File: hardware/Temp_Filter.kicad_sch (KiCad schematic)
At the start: 9 parts, among them U7 TLV9062xD

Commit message: schem except BQ
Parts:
- added C22: 1uF, Capacitor_SMD:C_0805_2012Metric_Pad1.18x1.45mm_HandSolder, symbol Device:C
- added C48: 1.2uF, Capacitor_SMD:C_0805_2012Metric_Pad1.18x1.45mm_HandSolder, symbol Device:C
- added R44: 27kΩ, Resistor_SMD:R_0603_1608Metric_Pad0.98x0.95mm_HandSolder, symbol Device:R
- added R45, R46: 2.7kΩ, Resistor_SMD:R_0603_1608Metric_Pad0.98x0.95mm_HandSolder, symbol Device:R
- added R9: 8.2kΩ, Resistor_SMD:R_0603_1608Metric_Pad0.98x0.95mm_HandSolder, symbol Device:R
- added TP12: TP_TempOut, TestPoint:TestPoint_Pad_1.0x1.0mm, symbol Connector:TestPoint
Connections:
- net GNDA: now also C22.2, R45.1
- net VDDA renamed 3.3VA
- net tempIn: no longer names the net of U7.3 (+)
- net tempIn: now also C22.1, R44.2
- net tempOut renamed tempOut_2
- new net: C48.1, R44.1, R9.2
- new net: R45.2, R46.1, U7.2 (-)
- new net tempIn_1: R9.1
- new net tempIn_2: R8.1
- new net tempOut_1: C48.2, R46.2, TP12.1, U7.1
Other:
- moved on the sheet: C20, C21, C47, R41, R42, R43, R8, TP11, U7B, U7C

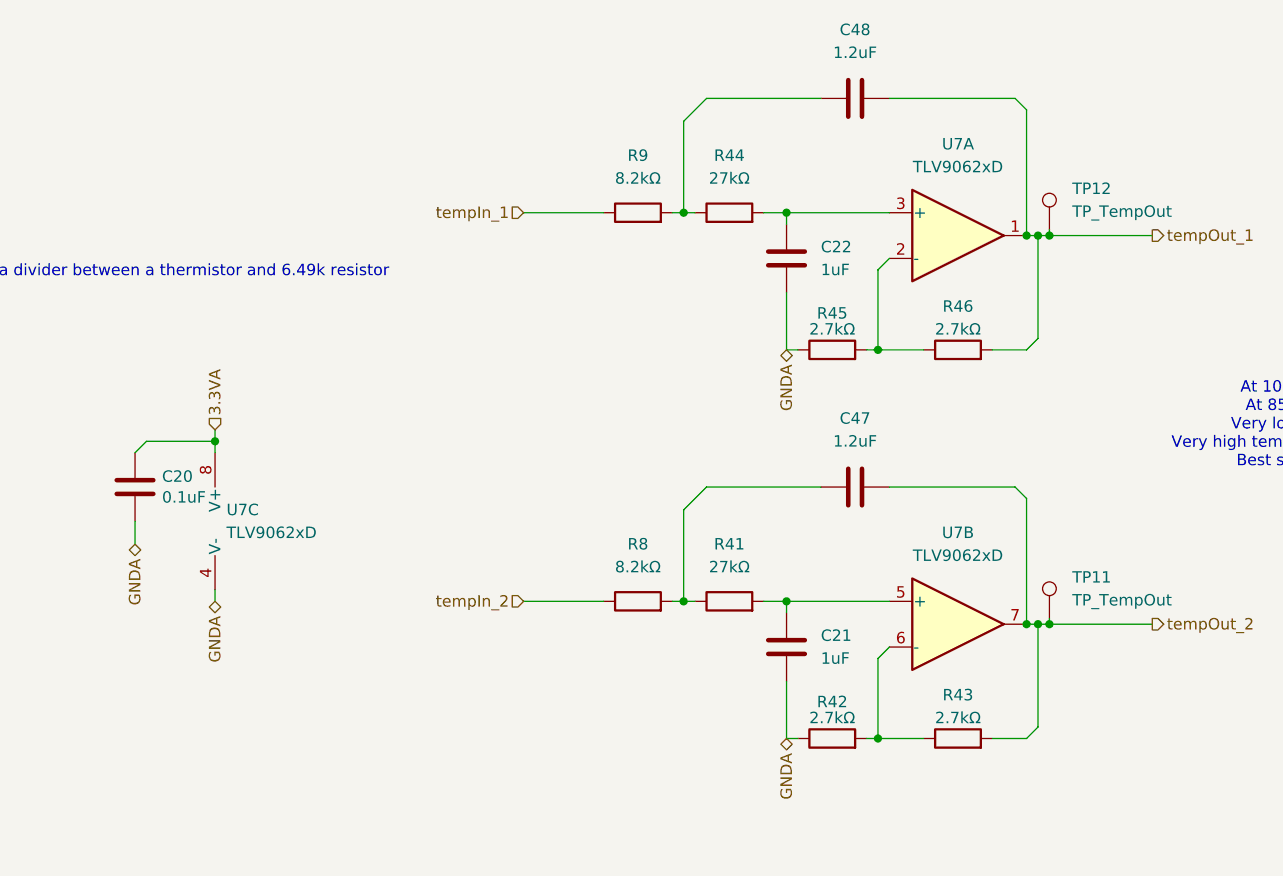
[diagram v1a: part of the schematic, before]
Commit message: New BMS arch and IC
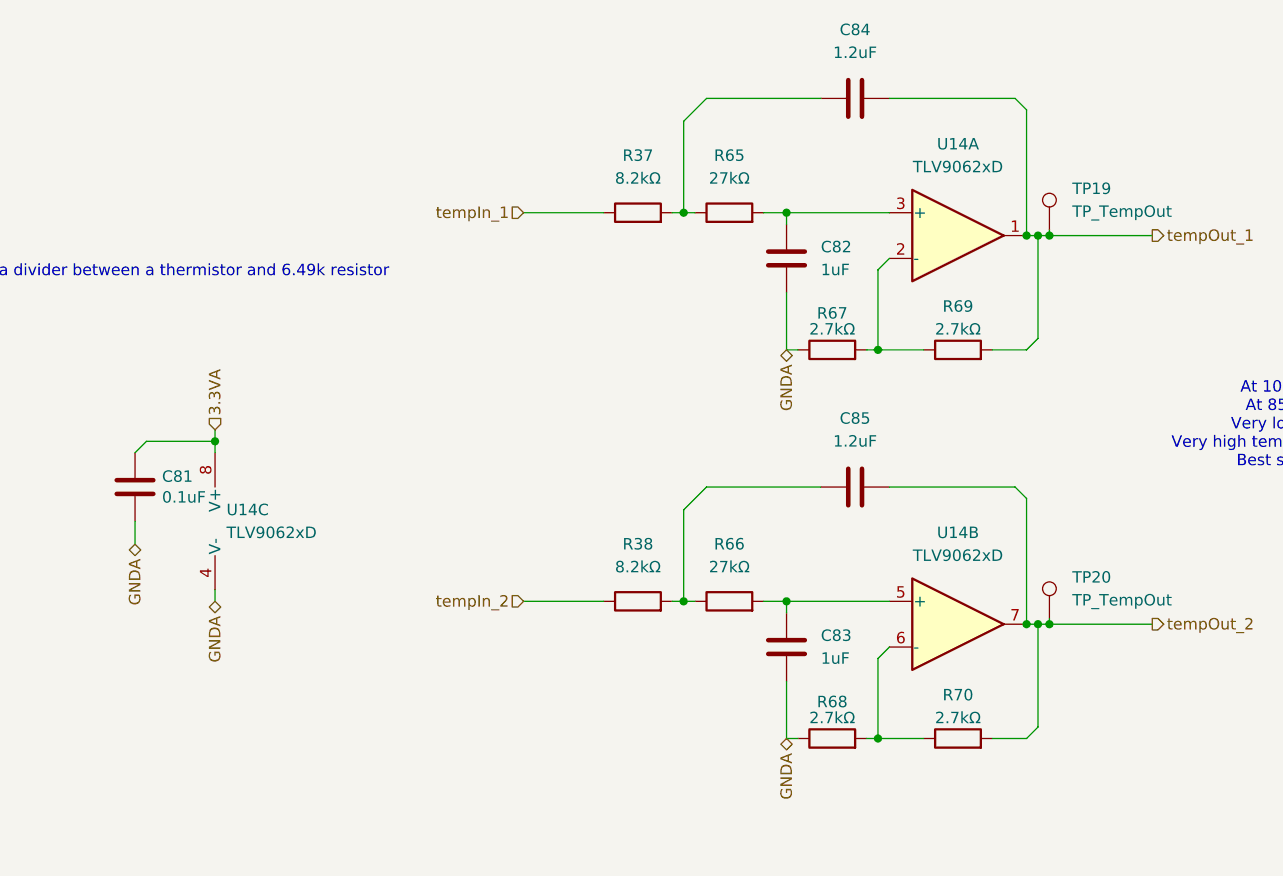
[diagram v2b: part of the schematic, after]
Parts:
- renumbered C20 to C81, C22 to C82, C21 to C83, C48 to C84, C47 to C85, R9 to R37, R8 to R38, R44 to R65, R41 to R66, R45 to R67, R42 to R68, R46 to R69, R43 to R70, TP12 to TP19, TP11 to TP20, U7 to U14
